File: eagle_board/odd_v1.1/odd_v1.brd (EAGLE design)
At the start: 100 x 40.6 mm, 17 parts

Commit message: Small changes.
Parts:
- U$1, U$2, U$3, U$4, U$5: value CREESMDRGBLED6PADSMD -> RGBLED
- moved IC1 1.27 mm to (47.0, 19.1)
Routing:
- net N$19: track 96.9 -> 99.5 mm
- net N$22: track 227.3 -> 228.6 mm
- net N$58: track 36.8 -> 38.1 mm
- net N$16: track 26.5 -> 25.2 mm
- net N$15: track 24.9 -> 23.7 mm
- net N$14: track 23.4 -> 22.1 mm
- net N$13: track 39.2 -> 37.9 mm
- net N$12: track 37.6 -> 36.4 mm
- net N$11: track 36.1 -> 34.8 mm
- net N$1: track 41.2 -> 39.9 mm
- net N$9: track 10.7 -> 9.41 mm
- net N$8: track 12.2 -> 10.9 mm
- net N$7: track 13.8 -> 12.5 mm
- net N$4: track 15.8 -> 14.5 mm
- net N$6: track 18.8 -> 17.6 mm
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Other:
- board size 100 x 40.6 mm -> 91.1 x 38.1 mm

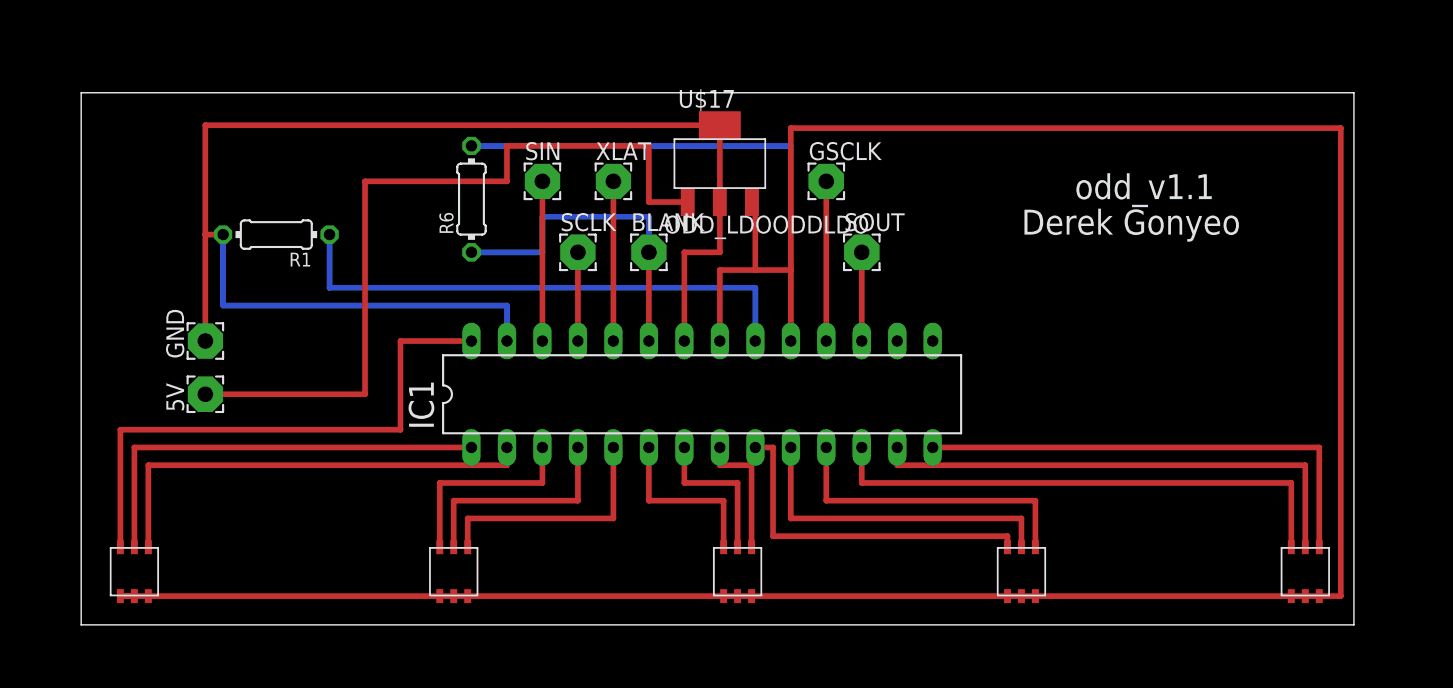
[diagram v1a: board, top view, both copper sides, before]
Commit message: Modified board, there were accidental and dumb connections being made. Also added two capacitors for use with the voltage regulator.
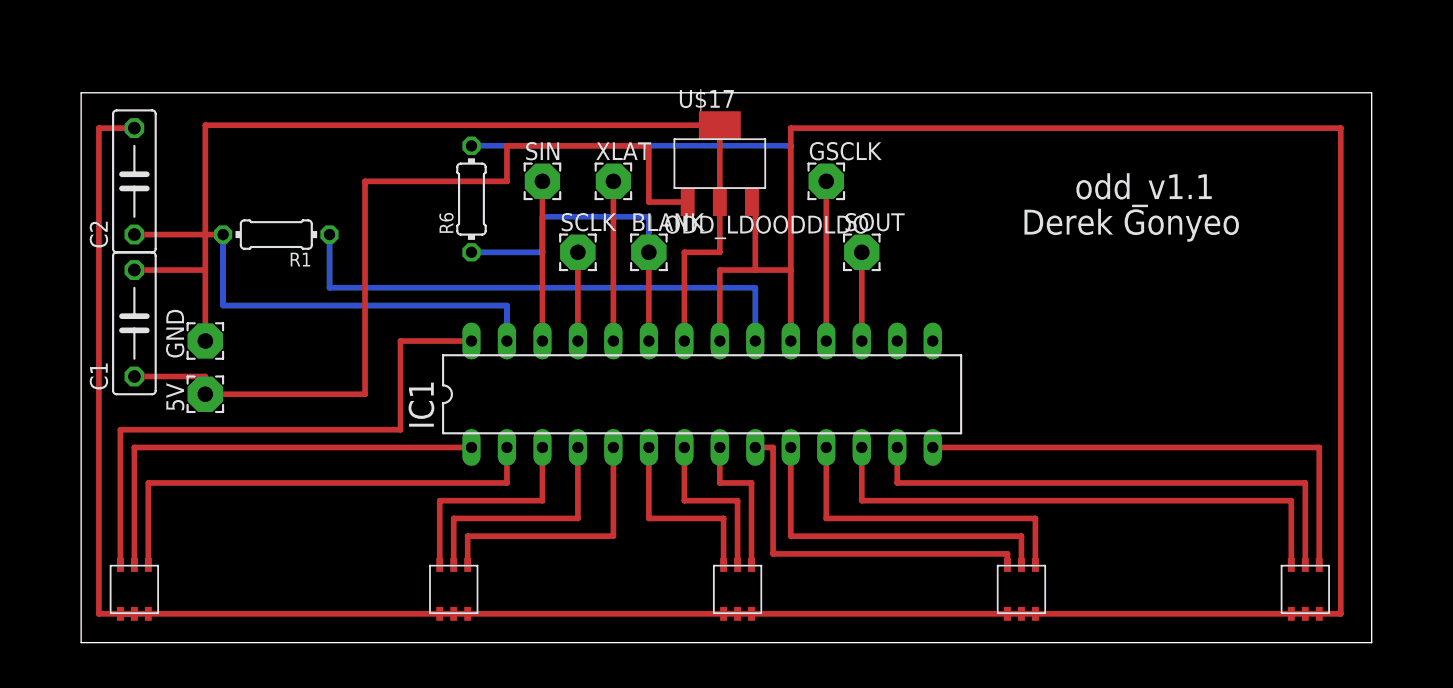
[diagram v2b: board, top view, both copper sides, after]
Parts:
- added C1, C2: (no value), resistor:C075-032X103
- moved U$1 1.27 mm to (7.62, 5.08)
- moved U$2 1.27 mm to (30.5, 5.08)
- moved U$3 1.27 mm to (50.8, 5.08)
- moved U$4 1.27 mm to (71.1, 5.08)
- moved U$5 1.27 mm to (91.4, 5.08)
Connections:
- net N$18: now also C1.1
- net N$19: now also C1.2, C2.1
- net N$22: now also C2.2
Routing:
- net N$22: track 228.6 -> 268.7 mm
- net N$19: track 99.5 -> 109.6 mm
- net N$18: track 56.3 -> 62.7 mm
- net N$15: track 23.7 -> 24.9 mm
- net N$13: track 37.9 -> 39.2 mm
- net N$9: track 9.41 -> 10.7 mm
- net N$8: track 10.9 -> 12.2 mm
- net N$7: track 12.5 -> 13.8 mm
- net N$6: track 17.6 -> 18.8 mm
- net N$5: track 16.0 -> 17.3 mm
- net N$4: track 14.5 -> 15.8 mm
- net N$2: track 31.3 -> 32.5 mm
- net N$16: track 25.2 -> 26.5 mm
- net N$3: track 32.8 -> 34.1 mm
- net N$14: track 22.1 -> 23.4 mm
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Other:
- board size 91.1 x 38.1 mm -> 92.4 x 39.4 mm

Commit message: Updated the board
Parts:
- moved C2 46.0 mm to (53.3, 29.2), turned to 180 degrees
- moved R1 41.3 mm to (58.4, 38.1)
- moved C1 39.1 mm to (45.7, 33.0), turned to 180 degrees
- moved 5V 31.8 mm to (38.1, 38.1)
- moved R6 26.7 mm to (58.4, 34.3), turned to 180 degrees
- moved GND 26.4 mm to (34.3, 38.1)
- moved GSCLK 7.62 mm to (57.1, 26.7)
- moved SIN 5.08 mm to (36.8, 29.2)
- moved XLAT 5.08 mm to (41.9, 29.2)
- moved U$17 3.81 mm to (49.5, 39.4)
- moved BLANK 2.54 mm to (44.5, 26.7)
- moved SCLK 2.54 mm to (39.4, 26.7)
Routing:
- net N$22: track 268.7 -> 173.1 mm
- net N$18: track 62.7 -> 23.3 mm
- net N$19: track 109.6 -> 76.5 mm
- net N$58: track 38.1 -> 25.3 mm
- net N$24: track 11.4 -> 3.81 mm
- net N$21: track 11.4 -> 6.35 mm
- net N$17: track 11.4 -> 6.35 mm
- net N$13: track 39.2 -> 34.2 mm
- net N$16: track 26.5 -> 21.5 mm
- net N$6: track 18.8 -> 13.9 mm
- net N$15: track 24.9 -> 20.5 mm
- net N$14: track 23.4 -> 19.3 mm
- net N$1: track 41.2 -> 37.1 mm
- net N$5: track 17.3 -> 13.6 mm
- net N$7: track 13.8 -> 10.6 mm
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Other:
- board size 92.4 x 39.4 mm -> 92.4 x 43.2 mm
